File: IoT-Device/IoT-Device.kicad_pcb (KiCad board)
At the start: 4 copper layers, 100 x 70 mm, 45 parts, among them J1 USB_C_Receptacle_USB2.0_16P, J2 Conn_ARM_JTAG_SWD_10, SW1 B1, SW2 B2, SW3 BOOT_MODE, SW4 RESET, U1 STM32U585VITx, U2 ESP32-C3-WROOM-02, U3 BD33GA5WEFJ

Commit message: add schematics, update metro shield
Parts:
- J1: value USB_C_Receptacle_USB2.0_16P -> USB-C
- J2: value Conn_ARM_JTAG_SWD_10 -> SWD
- U1: value STM32U585VITx -> STM32U585VI
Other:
- board text added: "B1"
- board text added: "B2"
- board text added: "BOOT_MODE"
- board text added: "ESP32-C3-WROOM-02"
- board text added: "PWR"
- board text added: "RESET"
- board text added: "RX"
- board text added: "STM32U585VI"
- board text added: "SWD"
- board text added: "TX"
- board text added: "USB-C"
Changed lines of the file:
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@@
 		)
 		(property "Value" "BOOT_MODE"
-			(at -7.5 -3.025 0)
+			(at -7.2 -3.225 0)
 			(layer "F.Fab")
 			(effects
@@
 		)
 		(property "Value" "RESET"
-			(at 0 4.15 0)
+			(at 0.1 3.5 0)
 			(layer "F.Fab")
 			(effects
@@
 		)
 		(property "Value" "B1"
-			(at 0 4.15 0)
+			(at 0 3.725 0)
 			(layer "F.Fab")
 			(effects
@@
 		)
 		(property "Value" "PWR"
-			(at 0 1.43 0)
+			(at 0 1.4 0)
 			(layer "F.Fab")
 			(effects
@@
 		)
 		(property "Value" "RX"
-			(at 0 1.43 0)
+			(at 0 1.35 0)
 			(layer "F.Fab")
 			(effects
@@
 			)
 		)
-		(property "Value" "STM32U585VITx"
+		(property "Value" "STM32U585VI"
 			(at 0.175 9.5 0)
 			(layer "F.Fab")
@@
 		)
 		(property "Value" "ESP32-C3-WROOM-02"
-			(at 0 8 90)
+			(at -1.34 8 90)
 			(layer "F.Fab")
 			(effects
@@
 			)
 		)
-		(property "Value" "Conn_ARM_JTAG_SWD_10"
-			(at 0 4.285 90)
+		(property "Value" "SWD"
+			(at -0.15 4.34 90)
 			(layer "F.Fab")
 			(effects
@@
 		)
 		(property "Value" "B2"
-			(at 0 4.15 0)
+			(at 0 3.7 0)
 			(layer "F.Fab")
 			(effects
@@
 			)
 		)
-		(property "Value" "USB_C_Receptacle_USB2.0_16P"
-			(at -6.4 -8.19 0)
+		(property "Value" "USB-C"
+			(at -5.9 0.01 0)
 			(unlocked yes)
 			(layer "F.Fab")
@@
 		)
 		(property "Value" "TX"
-			(at 0 1.43 0)
+			(at 0 1.4 0)
 			(layer "F.Fab")
 			(effects
@@
 		(layer "Edge.Cuts")
 	)
+	(gr_text "ESP32-C3-WROOM-02"
+		(at 46.3 69.9 90)
+		(layer "F.SilkS")
+		(effects
+			(font
+				(size 1 1)
+				(thickness 0.15)
+			)
+		)
+	)
+	(gr_text "RESET"
+		(at 65.1 57.5 0)
+		(layer "F.SilkS")
+		(effects
+			(font
+				(size 1 1)
+				(thickness 0.15)
+			)
+		)
+	)
+	(gr_text "BOOT_MODE"
+		(at 74 25.6 0)
+		(layer "F.SilkS")
+		(effects
+			(font
+				(size 1 1)
+				(thickness 0.15)
+			)
+		)
+	)
+	(gr_text "PWR"
+		(at 25.875 52 90)
+		(layer "F.SilkS")
+		(effects
+			(font
+				(size 1 1)
+				(thickness 0.15)
+			)
+		)
+	)
+	(gr_text "RX"
+		(at 25.85 47.8 90)
+		(layer "F.SilkS")
+		(effects
+			(font
+				(size 1 1)
+				(thickness 0.15)
+			)
+		)
+	)
+	(gr_text "B2"
+		(at 85.7 40.9 0)
+		(layer "F.SilkS")
+		(effects
+			(font
+				(size 1 1)
+				(thickness 0.15)
+			)
+		)
+	)
+	(gr_text "B1"
+		(at 94.9 40.925 0)
+		(layer "F.SilkS")
+		(effects
+			(font
+				(size 1 1)
+				(thickness 0.15)
+			)
+		)
+	)
+	(gr_text "TX"
+		(at 25.85 43.575 90)
+		(layer "F.SilkS")
+		(effects
+			(font
+				(size 1 1)
+				(thickness 0.15)
+			)
+		)
+	)
+	(gr_text "USB-C"
+		(at 28.7 26.6 0)
+		(layer "F.SilkS")
+		(effects
+			(font
+				(size 1 1)
+				(thickness 0.15)
+			)
+		)
+	)
+	(gr_text "STM32U585VI"
+		(at 88.5 68 0)
+		(layer "F.SilkS")
+		(effects
+			(font
+				(size 1 1)
+				(thickness 0.15)
+			)
+		)
+	)
+	(gr_text "SWD"
+		(at 120.2 31.6 90)
+		(layer "F.SilkS")
+		(effects
+			(font
+				(size 1 1)
+				(thickness 0.125)
+			)
+		)
+	)
 	(segment

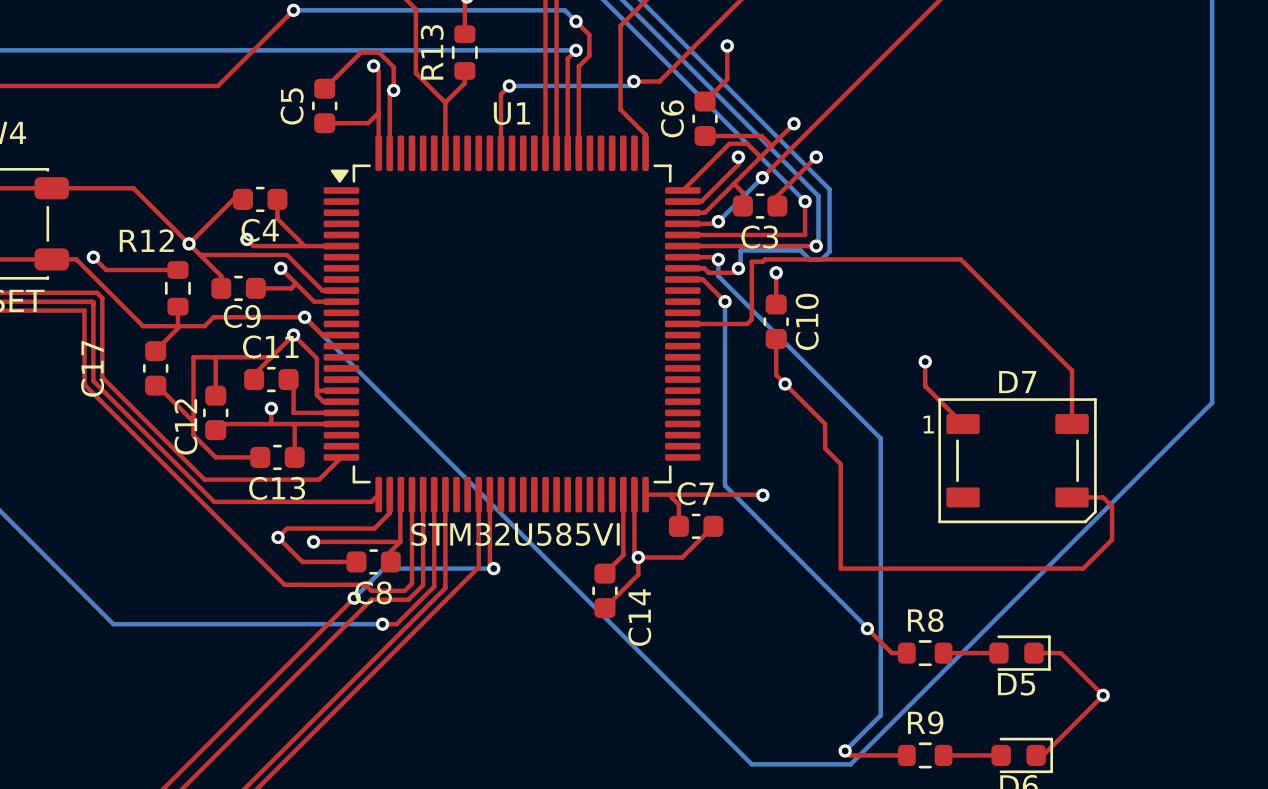
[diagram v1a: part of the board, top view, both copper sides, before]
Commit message: update IoT-device schematic, update pcb to free space around more pins
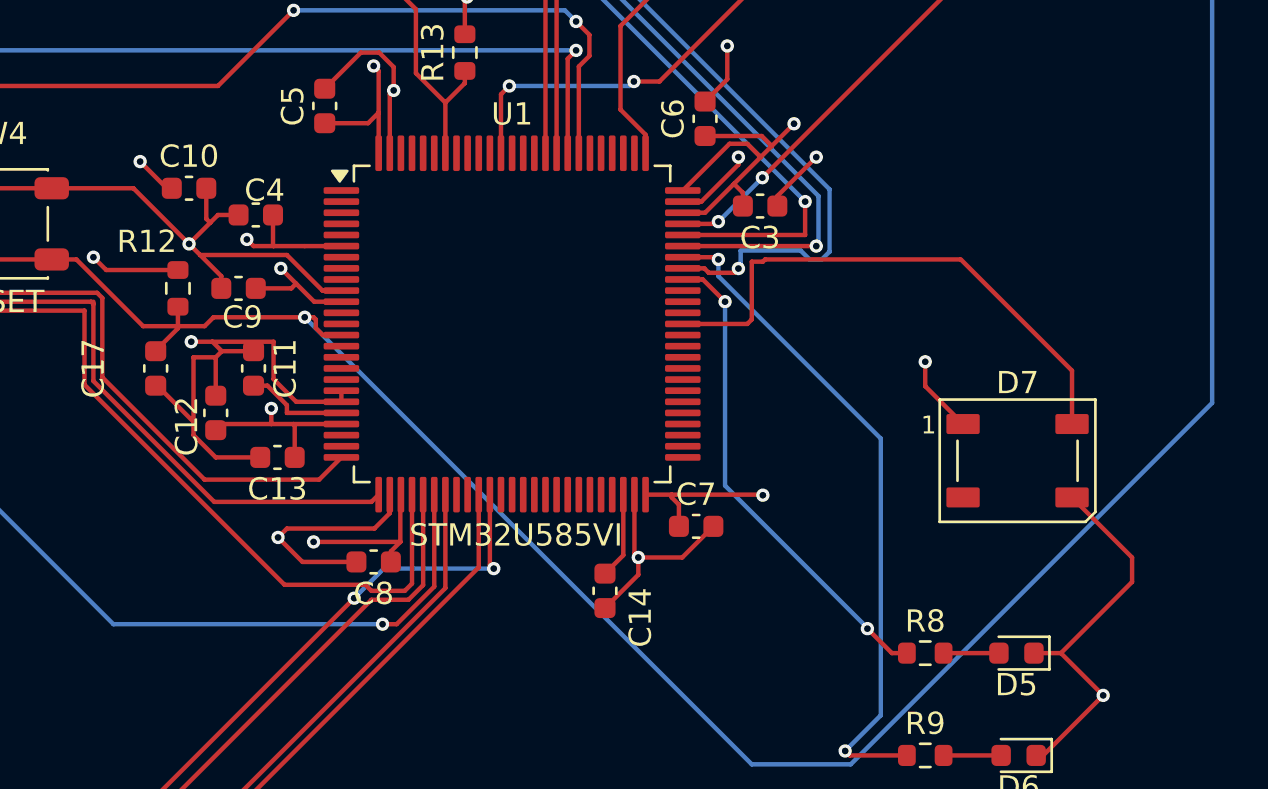
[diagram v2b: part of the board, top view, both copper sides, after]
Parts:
- C10: value 4.7uF -> 10uF
- moved C10 27.1 mm to (73.8, 52.4), turned to 0 degrees
- moved C11 0.94 mm to (76.7, 60.5), turned to -90 degrees
- moved C4 0.73 mm to (76.8, 53.6)
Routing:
- net GND: track 233.0 -> 216.9 mm, vias 22 -> 21
- net Net-(U1-VREF+): track 3.74 -> 4.66 mm
- net +3.3V: track 114.0 -> 113.3 mm

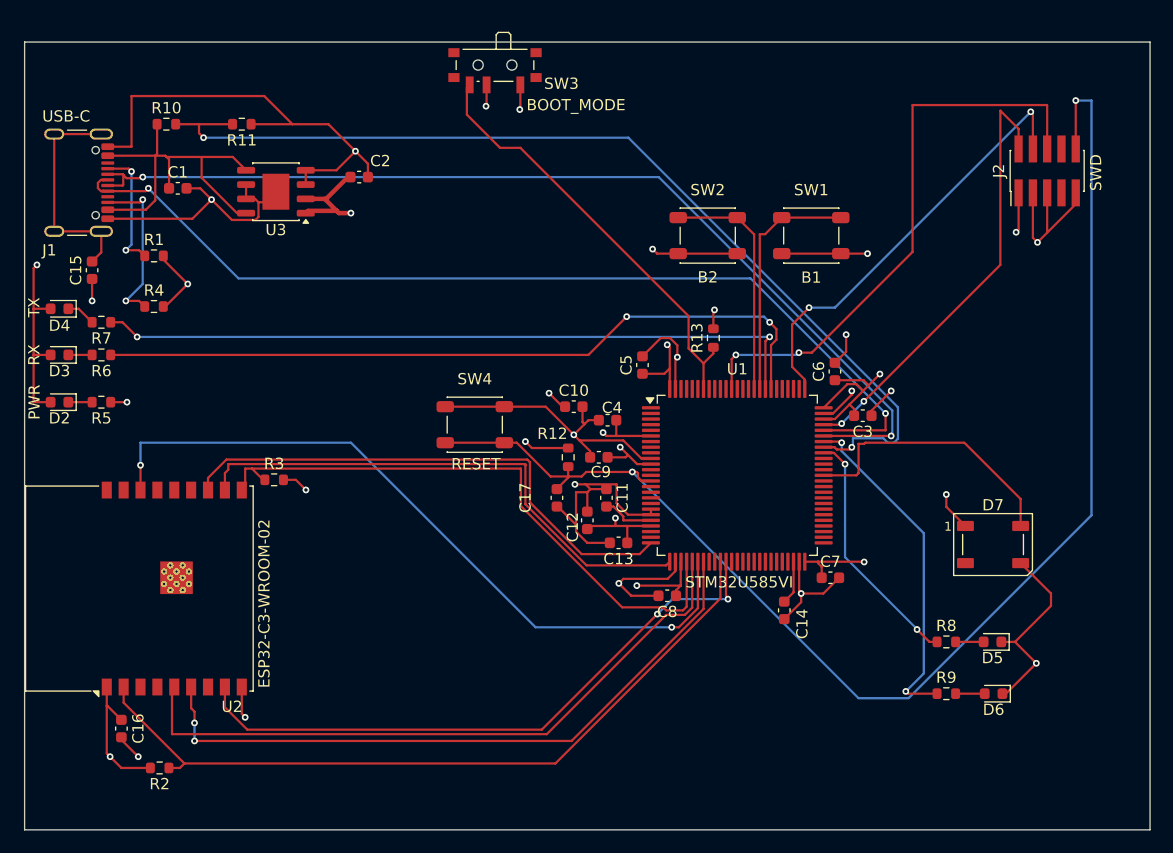
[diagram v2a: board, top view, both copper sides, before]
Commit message: add battery power to design
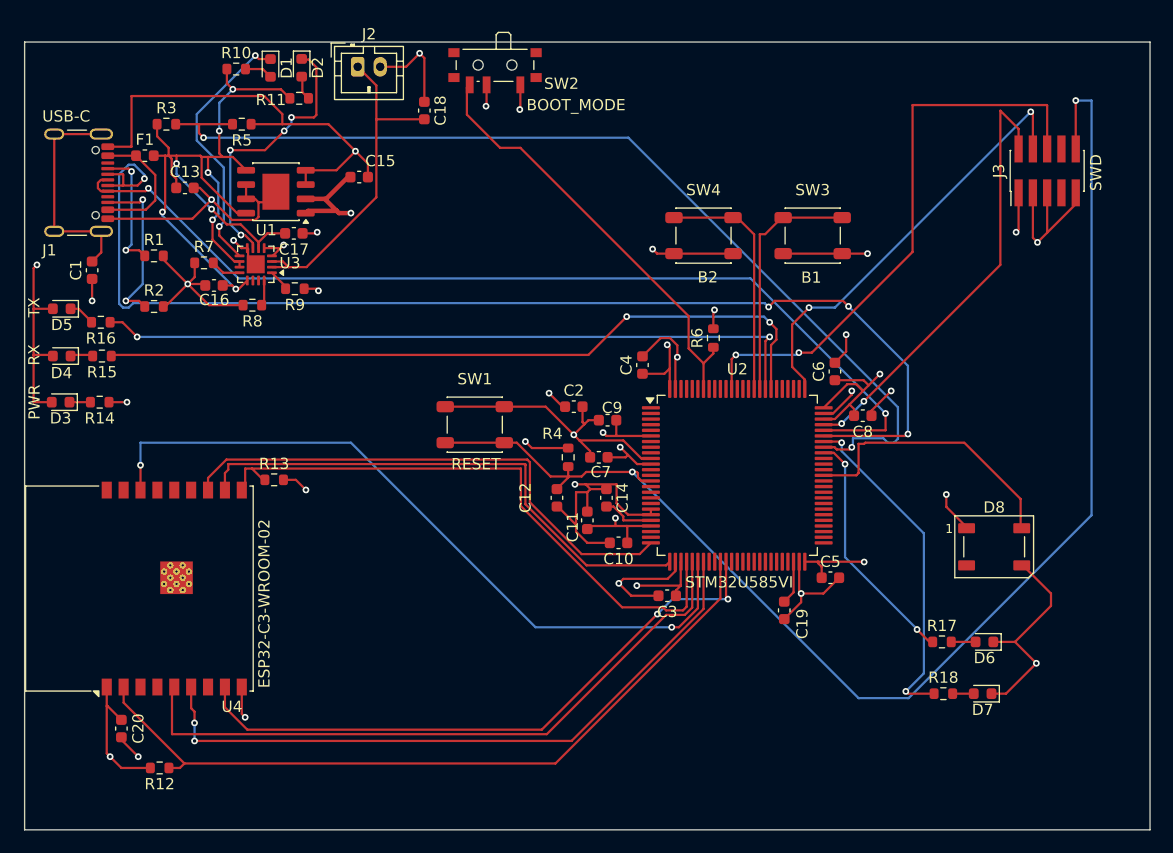
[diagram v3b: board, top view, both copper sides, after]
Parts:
- removed the R5 at (31.8, 52.0)
- removed the R6 at (31.8, 47.8)
- removed the SW1 at (94.9, 37.2)
- removed the SW2 at (85.7, 37.2)
- added C16: 4.7uF, Capacitor_SMD:C_0603_1608Metric, F.Cu at (41.8, 41.6)
- added C17: 4.7uF, Capacitor_SMD:C_0603_1608Metric, F.Cu at (48.9, 37.0)
- added C18: 4.7uF, Capacitor_SMD:C_0603_1608Metric, F.Cu at (60.5, 26.1)
- added D1: LED, LED_SMD:LED_0603_1608Metric, F.Cu at (46.9, 22.3)
- added D8: WS2812B, LED_SMD:LED_WS2812B_PLCC4_5.0x5.0mm_P3.2mm, F.Cu at (111.2, 64.8)
- added F1: Fuse, Fuse:Fuse_0603_1608Metric, F.Cu at (35.7, 30.1)
- added J2: Conn_01x02, Connector_JST:JST_PH_B2B-PH-K_1x02_P2.00mm_Vertical, F.Cu at (54.6, 22.2)
- added R10: 1k, Resistor_SMD:R_0603_1608Metric, F.Cu at (43.8, 22.4)
- added R11: 1k, Resistor_SMD:R_0603_1608Metric, F.Cu at (49.4, 25.0)
- added R14: 1k, Resistor_SMD:R_0603_1608Metric, F.Cu at (31.7, 52.0)
- added R15: 1k, Resistor_SMD:R_0603_1608Metric, F.Cu at (31.9, 47.9)
- added R16: 1k, Resistor_SMD:R_0603_1608Metric, F.Cu at (31.8, 44.9)
- added R17: 330, Resistor_SMD:R_0603_1608Metric, F.Cu at (106.5, 73.3)
- added R18: 330, Resistor_SMD:R_0603_1608Metric, F.Cu at (106.6, 77.9)
- added SW3: B1, Button_Switch_SMD:SW_SPST_PTS647_Sx50, F.Cu at (95.0, 37.2)
- added SW4: B2, Button_Switch_SMD:SW_SPST_PTS647_Sx50, F.Cu at (85.3, 37.2)
- added U3: BQ24074RGT, Package_DFN_QFN:VQFN-16-1EP_3x3mm_P0.5mm_EP1.6x1.6mm, F.Cu at (45.5, 39.8)
- D2: value PWR -> LED
- D3: value RX -> PWR
- D4: value TX -> RX
- D5: value LED -> TX
- D7: value WS2812B -> LED; footprint LED_SMD:LED_WS2812B_PLCC4_5.0x5.0mm_P3.2mm -> LED_SMD:LED_0603_1608Metric
- R7: value 1k -> 3.2k
- R8: value 330 -> 1.8k
- R9: value 330 -> 10k
- moved D5 87.8 mm to (28.3, 43.7)
- moved R8 68.5 mm to (45.2, 43.4), turned to 180 degrees
- moved R9 68.2 mm to (49.0, 41.9), turned to 180 degrees
- moved D2 36.7 mm to (49.6, 22.3), turned to -90 degrees
- moved D7 13.3 mm to (110.1, 77.9), turned to 180 degrees
- moved R7 10.5 mm to (40.9, 39.6), turned to 0 degrees
- moved D6 4.67 mm to (110.3, 73.3)
- moved D4 4.20 mm to (28.3, 47.9)
- moved D3 4.20 mm to (28.2, 52.0)
- moved C13 0.64 mm to (39.2, 33.0)
- renumbered C15 to C1, C13 to C10, C12 to C11, C17 to C12, C1 to C13, C11 to C14, C2 to C15, C14 to C19, C10 to C2, C16 to C20, C8 to C3, C5 to C4, C7 to C5, C9 to C7, C3 to C8, C4 to C9, J2 to J3, R2 to R12, R3 to R13, R4 to R2, R10 to R3, R12 to R4, R11 to R5, R13 to R6, SW4 to SW1, SW3 to SW2, U3 to U1, U1 to U2, U2 to U4
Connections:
- C13 pad 1: /+5V_USB -> /SYS
- D2 pad 2: +3.3V -> Net-(D2-A)
- D5 pad 1: GND -> Net-(D5-K)
- D5 pad 2: Net-(D5-A) -> +3.3V
- D7 pad 1: +3.3V -> GND
- D7 pad 2: unconnected-(D7-DOUT-Pad2) -> Net-(D7-A)
- R3 pad 1: /+5V_USB -> /SYS
- R7 pad 1: /TX_LED -> GND
- R7 pad 2: Net-(D4-K) -> Net-(U3-ILIM)
- R8 pad 1: /LED1 -> Net-(U3-ISET)
- R8 pad 2: Net-(D5-A) -> GND
- R9 pad 1: /LED2 -> GND
- R9 pad 2: Net-(D6-A) -> Net-(U3-TS)
- U1 pad 5: /+5V_USB -> /SYS
- U1 pad 8: /+5V_USB -> /SYS
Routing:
- net /SYS: track 0.00 -> 79.8 mm, vias 0 -> 8
- net /BAT: track 0.00 -> 30.1 mm
- net GND: track 216.9 -> 244.4 mm, vias 21 -> 26
- net Net-(D1-K): track 0.00 -> 23.3 mm, vias 0 -> 2
- net Net-(D2-K): track 2.11 -> 24.8 mm, vias 0 -> 4
- net /+5V_USB: track 33.1 -> 11.3 mm
- net /OTG_DM: track 88.1 -> 106.5 mm, vias 2 -> 4
- net Net-(U3-ILIM): track 0.00 -> 2.70 mm
- net Net-(D5-K): track 0.00 -> 2.61 mm
- net Net-(D1-A): track 0.00 -> 2.51 mm
- net Net-(D5-A): track 2.49 -> 0.00 mm
- net Net-(U3-ISET): track 0.00 -> 2.28 mm
- net Net-(D2-A): track 0.00 -> 2.09 mm
- net Net-(U3-TS): track 0.00 -> 1.92 mm
- net Net-(D7-A): track 0.00 -> 1.88 mm
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
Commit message: fix ESP32 (GPIO2 & GPIO9) issue on schematic
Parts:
- added R19: 10k, Resistor_SMD:R_0603_1608Metric, F.Cu at (35.3, 56.8)
- added R20: 10k, Resistor_SMD:R_0603_1608Metric, F.Cu at (46.7, 79.3)
- moved J3 5.48 mm to (118.2, 26.5), turned to 180 degrees
- moved R12 0.15 mm to (36.9, 84.5), turned to 0 degrees
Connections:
- R12 pad 1: /ESP_RESET -> +3.3V
- R12 pad 2: +3.3V -> /ESP_RESET
- U4 pad 16: /SPI1_MISO -> Net-(U4-IO2)
- U4 pad 3: unconnected-(U4-IO4-Pad3) -> /SPI1_MISO
- U4 pad 4: unconnected-(U4-IO5-Pad4) -> /ESP_BUSY
- U4 pad 8: /ESP_BUSY -> Net-(U4-IO9)
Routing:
- net /ESP_BUSY: track 55.5 -> 63.8 mm
- net /SWO: track 51.6 -> 43.6 mm
- net /SPI1_MISO: track 65.4 -> 59.0 mm
- net Net-(U4-IO9): track 0.00 -> 6.27 mm
- net /SWDIO: track 39.4 -> 34.2 mm
- net GND: track 244.4 -> 240.1 mm
- net +3.3V: track 113.3 -> 116.2 mm, vias 16 -> 18
- net Net-(U4-IO2): track 0.00 -> 2.18 mm
- net /MCU_RESET: track 121.1 -> 123.1 mm
- net /SWCLK: track 38.6 -> 36.9 mm

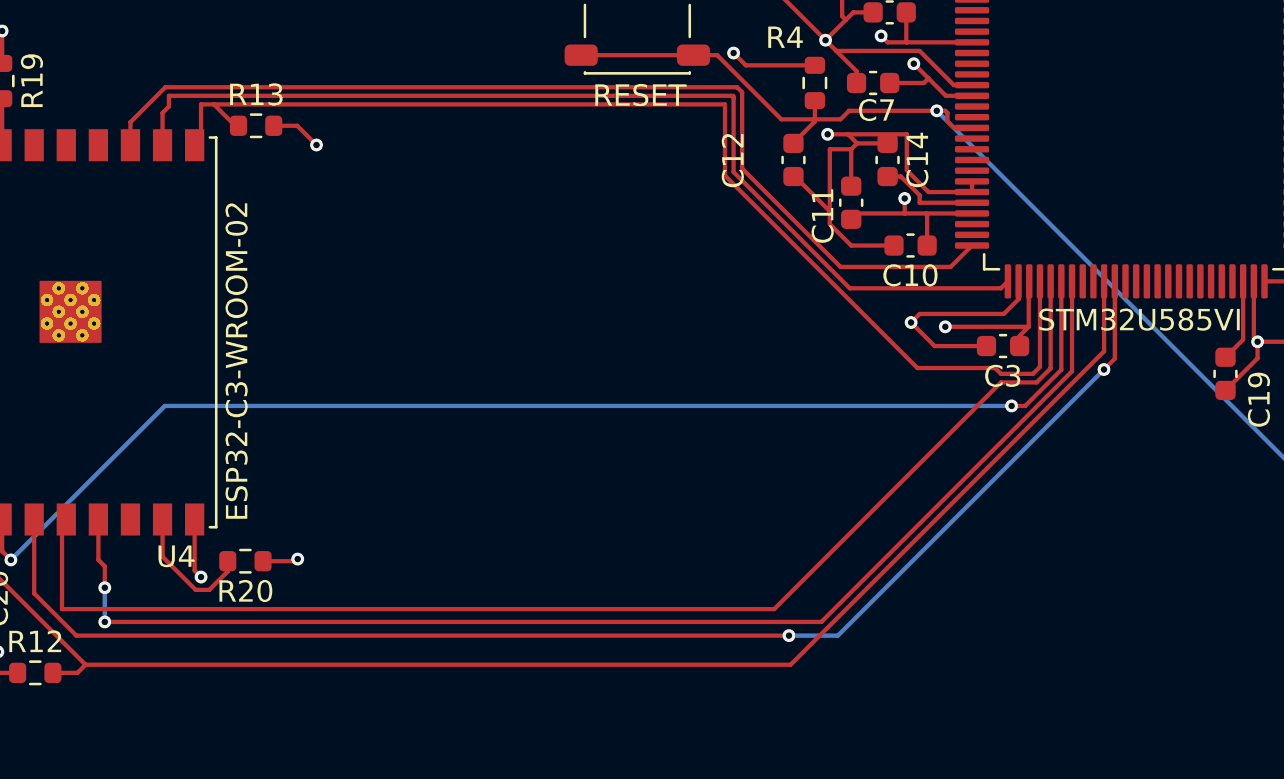
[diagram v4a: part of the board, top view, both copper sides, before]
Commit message: update schematic and PCB to allow ESP32-C3 boot mode change via STM32
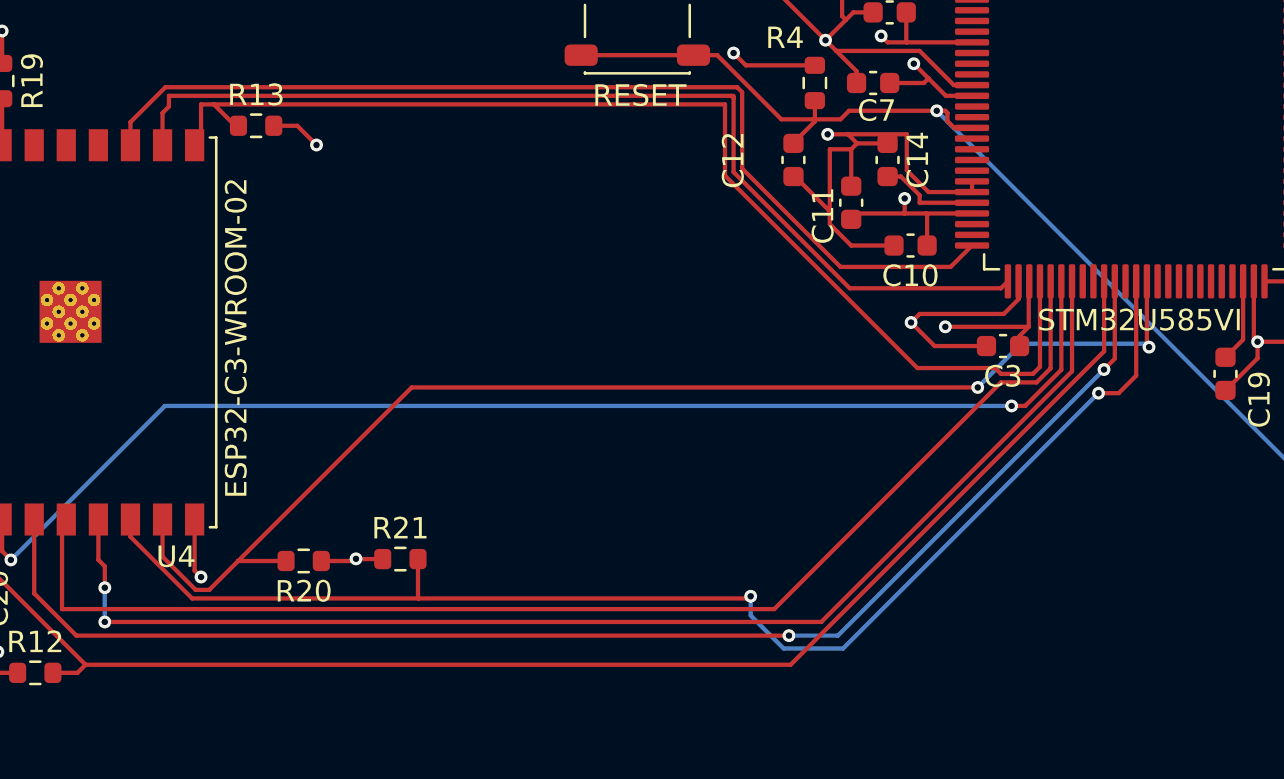
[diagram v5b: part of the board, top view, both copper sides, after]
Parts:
- added R21: 10k, Resistor_SMD:R_0603_1608Metric, F.Cu at (53.9, 79.2)
- moved R20 2.73 mm to (49.4, 79.2)
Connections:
- R20 pad 2: Net-(U4-IO9) -> /ESP_GPIO9
- U2 pad 38: unconnected-(U2-PE7-Pad38) -> /ESP_GPIO8
- U2 pad 39: unconnected-(U2-PE8-Pad39) -> /ESP_GPIO9
- U4 pad 7: unconnected-(U4-IO8-Pad7) -> /ESP_GPIO8
- U4 pad 8: Net-(U4-IO9) -> /ESP_GPIO9
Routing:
- net /ESP_GPIO8: track 0.00 -> 62.2 mm, vias 0 -> 2
- net /ESP_GPIO9: track 0.00 -> 58.7 mm, vias 0 -> 2
- net Net-(U4-IO9): track 6.27 -> 0.00 mm
- net +3.3V: track 116.2 -> 117.5 mm
